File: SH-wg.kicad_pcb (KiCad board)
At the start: 4 copper layers, 54.6 x 99.2 mm, 83 parts, among them J101 Aux PCB Conn Male, J102 Aux PCB Conn Female, J201 Conn_01x05, J301 JTAG, J302 Digital IO, J303 Analog IO, J401 Power, J501 Conn_01x04, J701 Conn_02x03_Odd_Even, Q801 2N7002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

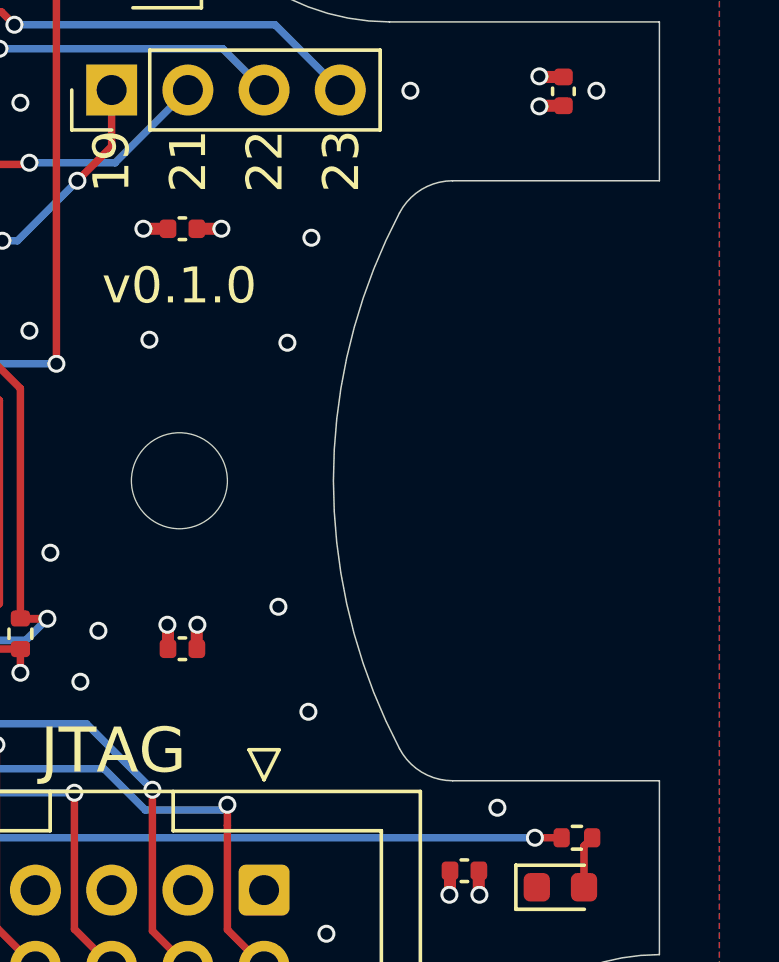
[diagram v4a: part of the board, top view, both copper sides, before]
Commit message: Add copper clearance around the mounting hole
Also make the M12 connector opening 1.5mm wider.
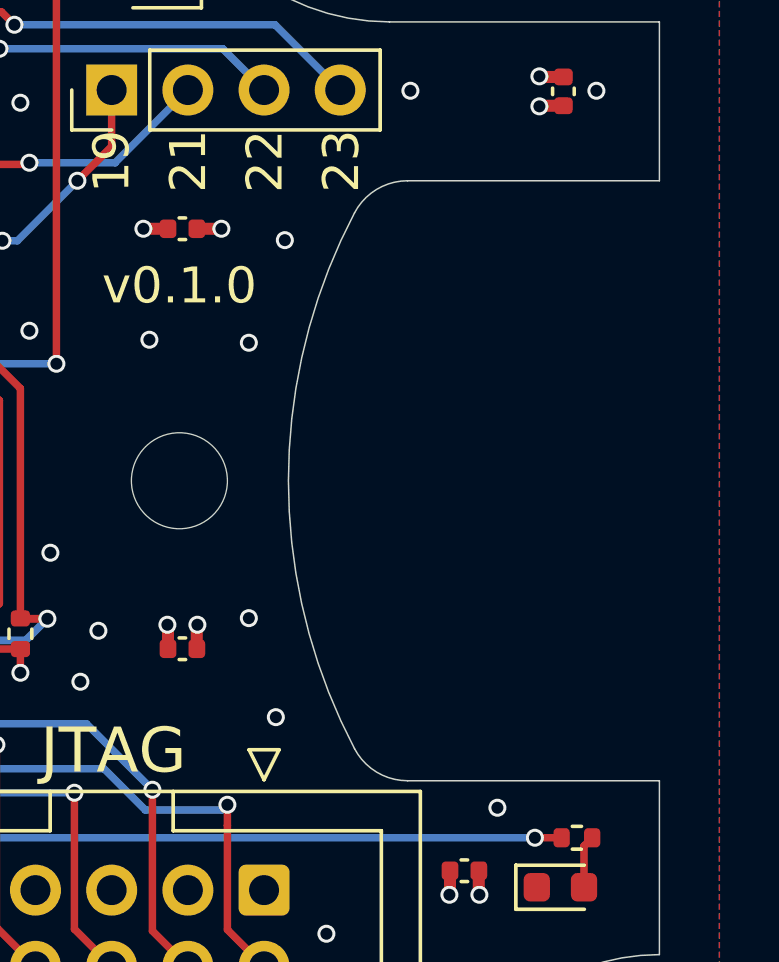
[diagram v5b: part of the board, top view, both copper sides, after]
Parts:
- H404: footprint MountingHole:MountingHole_3.2mm_M3 -> SH-wg:MountingHole_3.2mm_M3_no_copper
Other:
- outline, holes or cut-outs redrawn
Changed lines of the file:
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@@
     )
   )
-  (footprint "MountingHole:MountingHole_3.2mm_M3" (layer "F.Cu")
+  (footprint "SH-wg:MountingHole_3.2mm_M3_no_copper" (layer "F.Cu")
     (at 80.285 57.62)
     (descr "Mounting Hole 3.2mm, no annular, M3")
@@
     (fp_circle (center 0 0) (end 3.2 0) (layer "Cmts.User") (width 0.15) (fill none))
     (fp_circle (center 0 0) (end 3.45 0) (layer "F.CrtYd") (width 0.05) (fill none))
-    (pad "" np_thru_hole circle (at 0 0) (size 3.2 3.2) (drill 3.2) (layers *.Cu *.Mask))
+    (pad "" np_thru_hole circle (at 0 0) (size 3.2 3.2) (drill 3.2) (layers F&B.Cu *.Mask)
+      (solder_mask_margin 1.4) (clearance 1.6))
   )
   (footprint "Resistor_SMD:R_0402_1005Metric" (layer "F.Cu")
@@
   (gr_arc (start 96.285002 41.271847) (mid 98.29895 42.106052) (end 99.133155 44.12) (layer "Dwgs.User") (width 0.2))
   (gr_arc (start 87.285 41.271847) (mid 82.581434 39.323566) (end 80.633153 34.62) (layer "Dwgs.User") (width 0.2))
-  (gr_arc (start 87.622578 66.550309) (mid 85.419148 57.62) (end 87.622578 48.689691) (layer "Edge.Cuts") (width 0.05))
+  (gr_arc (start 86.122578 66.550309) (mid 83.919148 57.62) (end 86.122578 48.689691) (layer "Edge.Cuts") (width 0.05))
   (gr_line (start 43 116.62) (end 43 138.62) (layer "Edge.Cuts") (width 0.05))
   (gr_arc (start 44.285 72.914919) (mid 43.015801 72.389199) (end 42.490081 71.12) (layer "Edge.Cuts") (width 0.05))
@@
   (gr_arc (start 49.785 39.37) (mid 47.296537 41.183449) (end 44.285 41.825081) (layer "Edge.Cuts") (width 0.05))
   (gr_arc (start 89.079919 80.62) (mid 88.554199 81.889199) (end 87.285 82.414919) (layer "Edge.Cuts") (width 0.05))
-  (gr_arc (start 89.393037 67.62) (mid 88.358778 67.331814) (end 87.622578 66.550309) (layer "Edge.Cuts") (width 0.05))
+  (gr_arc (start 87.893037 67.62) (mid 86.858778 67.331814) (end 86.122578 66.550309) (layer "Edge.Cuts") (width 0.05))
   (gr_line (start 87.285 82.414919) (end 62.785 82.414919) (layer "Edge.Cuts") (width 0.05))
   (gr_arc (start 87.285 42.325081) (mid 83.940882 41.546238) (end 81.285 39.37) (layer "Edge.Cuts") (width 0.05))
   (gr_arc (start 53.285 72.914919) (mid 58.733315 75.171685) (end 60.990081 80.62) (layer "Edge.Cuts") (width 0.05))
   (gr_line (start 96.284999 67.62) (end 96.285 73.414919) (layer "Edge.Cuts") (width 0.05))
-  (gr_arc (start 87.622578 48.689691) (mid 88.358779 47.908186) (end 89.393037 47.62) (layer "Edge.Cuts") (width 0.05))
+  (gr_arc (start 86.122578 48.689691) (mid 86.858779 47.908186) (end 87.893037 47.62) (layer "Edge.Cuts") (width 0.05))
   (gr_arc (start 62.785 82.414919) (mid 61.515801 81.889199) (end 60.990081 80.62) (layer "Edge.Cuts") (width 0.05))
   (gr_line (start 97.08 116.62) (end 43 116.62) (layer "Edge.Cuts") (width 0.05))
@@
   (gr_line locked (start 49.785 39.37) (end 81.285 39.37) (layer "Edge.Cuts") (width 0.05))
   (gr_line (start 42.490081 71.12) (end 42.490081 43.62) (layer "Edge.Cuts") (width 0.05))
-  (gr_line (start 89.393037 67.62) (end 96.284999 67.62) (layer "Edge.Cuts") (width 0.05))
-  (gr_line (start 96.284999 47.62) (end 89.393037 47.62) (layer "Edge.Cuts") (width 0.05))
+  (gr_line (start 87.893037 67.62) (end 96.284999 67.62) (layer "Edge.Cuts") (width 0.05))
+  (gr_line (start 96.284999 47.62) (end 87.893037 47.62) (layer "Edge.Cuts") (width 0.05))
   (gr_text "SDA" (at 52.985 131.42 180) (layer "B.SilkS")
     (effects (font (size 0.8 0.8) (thickness 0.15)) (justify left mirror))
@@
   (via (at 60.485 75.22) (size 0.6) (drill 0.4) (layers "F.Cu" "B.Cu") (free) (net 1))
   (via (at 70.985 81.32) (size 0.6) (drill 0.4) (layers "F.Cu" "B.Cu") (free) (net 1))
-  (via (at 83.585 61.82) (size 0.6) (drill 0.4) (layers "F.Cu" "B.Cu") (free) (net 1))
+  (via (at 82.6 62.2) (size 0.6) (drill 0.4) (layers "F.Cu" "B.Cu") (free) (net 1))
   (via (at 58.085 60.82) (size 0.8) (drill 0.4) (layers "F.Cu" "B.Cu") (net 1))
   (via (at 68.585 49.92) (size 0.6) (drill 0.4) (layers "F.Cu" "B.Cu") (free) (net 1))
@@
   (via (at 92.285 45.14) (size 0.6) (drill 0.4) (layers "F.Cu" "B.Cu") (net 1))
   (via (at 50.485 50.62) (size 0.6) (drill 0.4) (layers "F.Cu" "B.Cu") (net 1))
-  (via (at 83.885 53.02) (size 0.6) (drill 0.4) (layers "F.Cu" "B.Cu") (free) (net 1))
+  (via (at 82.6 53.02) (size 0.6) (drill 0.4) (layers "F.Cu" "B.Cu") (free) (net 1))
   (via (at 80.285 79.62) (size 0.6) (drill 0.4) (layers "F.Cu" "B.Cu") (net 1))
   (via (at 62.285 51.72) (size 0.6) (drill 0.4) (layers "F.Cu" "B.Cu") (free) (net 1))
   (via (at 75.985 60.02) (size 0.6) (drill 0.4) (layers "F.Cu" "B.Cu") (free) (net 1))
   (via (at 89.285 71.42) (size 0.6) (drill 0.4) (layers "F.Cu" "B.Cu") (net 1))
-  (via (at 84.685 49.52) (size 0.6) (drill 0.4) (layers "F.Cu" "B.Cu") (free) (net 1))
+  (via (at 83.8 49.6) (size 0.6) (drill 0.4) (layers "F.Cu" "B.Cu") (free) (net 1))
   (via (at 70.585 63.82) (size 0.6) (drill 0.4) (layers "F.Cu" "B.Cu") (free) (net 1))
   (via (at 62.085 78.52) (size 0.6) (drill 0.4) (layers "F.Cu" "B.Cu") (free) (net 1))
@@
   (via (at 70.985 79.62) (size 0.6) (drill 0.4) (layers "F.Cu" "B.Cu") (net 1))
   (via (at 45.985 47.22) (size 0.6) (drill 0.4) (layers "F.Cu" "B.Cu") (net 1))
-  (via (at 84.585 65.32) (size 0.6) (drill 0.4) (layers "F.Cu" "B.Cu") (free) (net 1))
+  (via (at 83.5 65.5) (size 0.6) (drill 0.4) (layers "F.Cu" "B.Cu") (free) (net 1))
   (via (at 76.985 64.32) (size 0.6) (drill 0.4) (layers "F.Cu" "B.Cu") (free) (net 1))
   (via (at 79.085 49.22) (size 0.6) (drill 0.4) (layers "F.Cu" "B.Cu") (net 1))

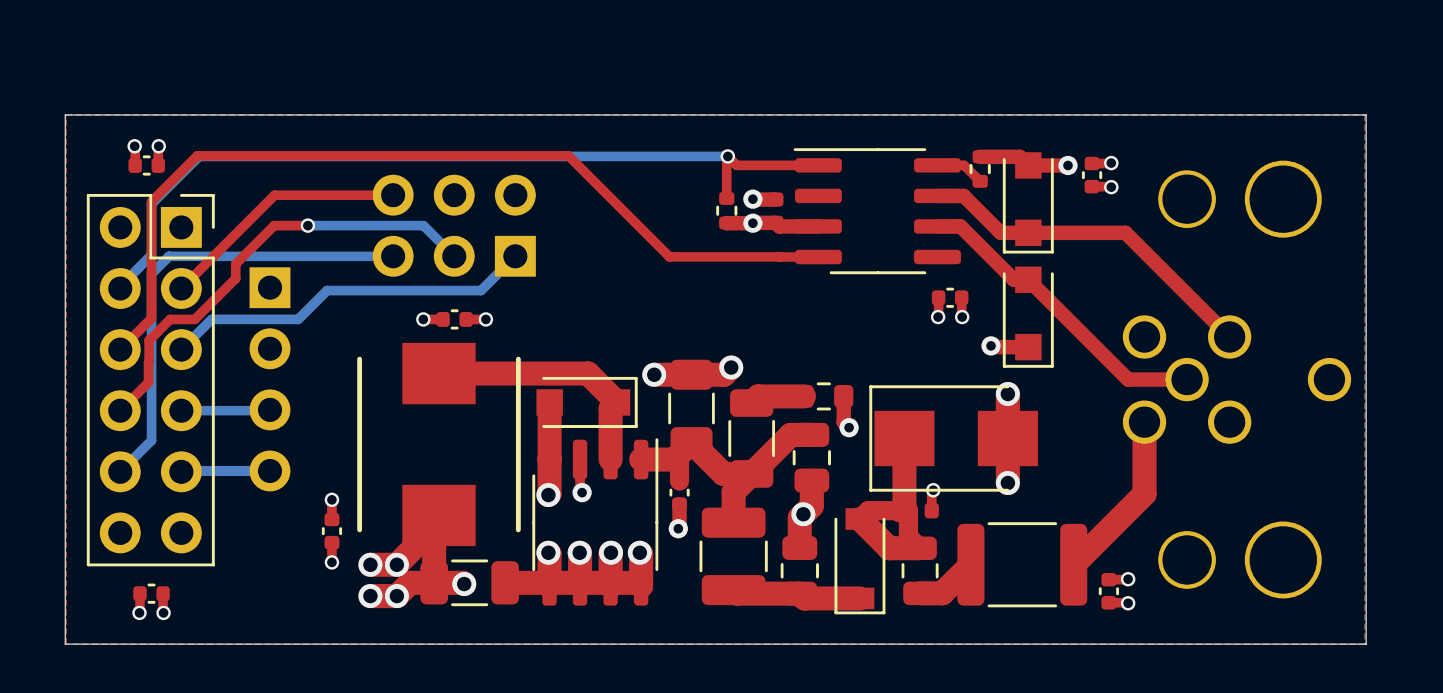
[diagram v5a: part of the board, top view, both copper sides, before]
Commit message: Update the design based on the test results
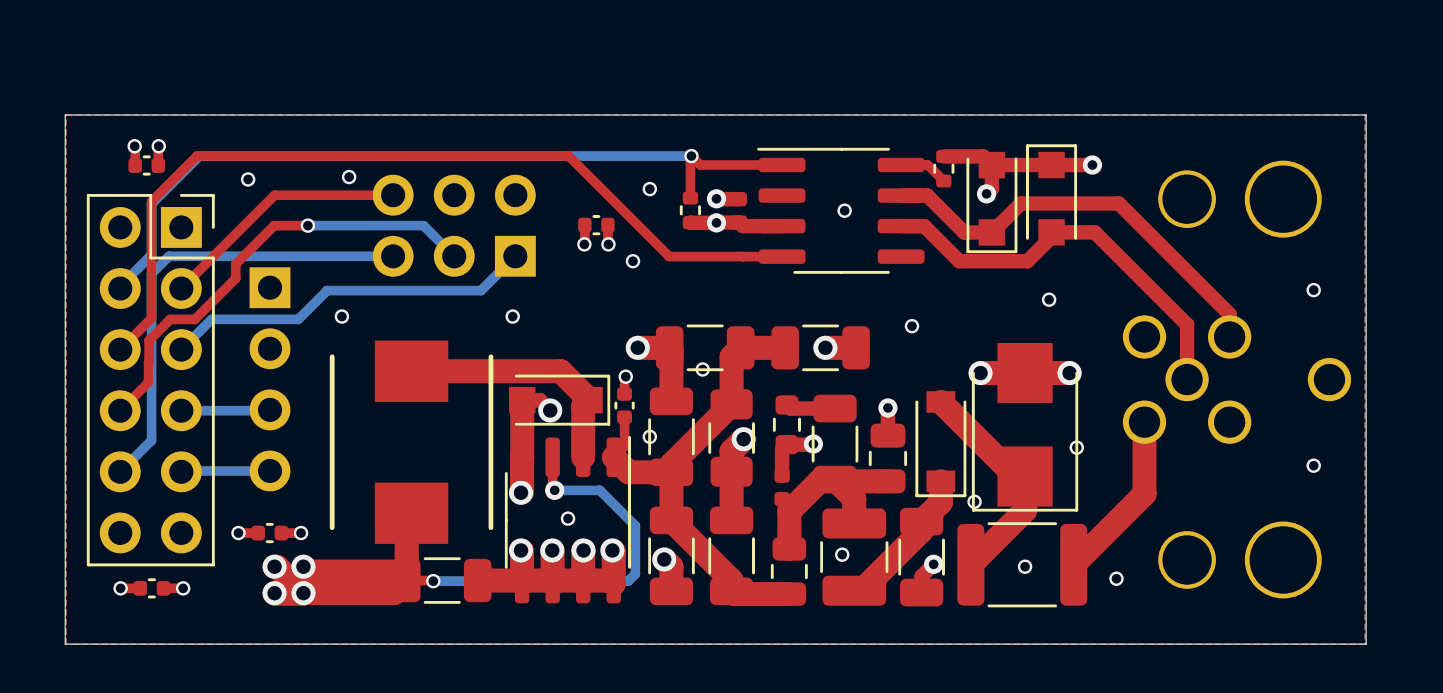
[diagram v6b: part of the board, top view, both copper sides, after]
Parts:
- removed C702, C703, C705: 100nF, Capacitor_SMD:C_0402_1005Metric
- added C608: 10uF/50V, Capacitor_SMD:C_1206_3216Metric, F.Cu at (69.6, 126.3)
- added C609: 10uF/50V, Capacitor_SMD:C_1206_3216Metric, F.Cu at (74.4, 126.3)
- added C610: 10uF/50V, Capacitor_SMD:C_1206_3216Metric, F.Cu at (70.7, 134.9)
- added C611: 10uF/50V, Capacitor_SMD:C_1206_3216Metric, F.Cu at (68.2, 130.0)
- added C612: 10uF/50V, Capacitor_SMD:C_1206_3216Metric, F.Cu at (68.2, 134.9)
- C601: value 470nF/50V -> 10uF/50V; footprint Capacitor_SMD:C_0805_2012Metric -> Capacitor_SMD:C_1206_3216Metric
- C602: value 10nF/50V -> 4.7nF/50V
- C605: value 22uF/35V -> 10uF/50V
- moved C704 15.0 mm to (65.1, 121.2)
- moved C707 11.7 mm to (51.5, 134.0)
- moved C701 7.85 mm to (46.6, 136.3), turned to 0 degrees
- moved D602 5.92 mm to (79.4, 130.2)
- moved C602 5.82 mm to (72.8, 132.1), turned to 90 degrees
- moved FB601 5.44 mm to (73.1, 135.6), turned to 90 degrees
- moved C601 5.10 mm to (78.6, 135.0), turned to 90 degrees
- moved L601 5.02 mm to (75.8, 135.0)
- moved D202 4.87 mm to (84.0, 120.1), turned to -90 degrees
- moved C606 4.28 mm to (66.2, 128.7), turned to 90 degrees
- moved C604 3.47 mm to (75.0, 130.3)
- moved C603 3.17 mm to (77.2, 130.9), turned to -90 degrees
- moved D601 2.92 mm to (82.9, 129.5), turned to 90 degrees
- moved C605 2.07 mm to (70.7, 130.1), turned to -90 degrees
- moved R601 1.94 mm to (73.0, 129.5), turned to 90 degrees
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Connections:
- C602 pad 1: /Power input/Vin_fused -> Net-(C602-Pad1)
- C603 pad 2: /Power input/IN -> Net-(C602-Pad1)
- C604 pad 1: /Power input/IN -> Net-(C602-Pad1)
- F601 pad 1: Net-(F601-Pad1) -> /Power input/Vin_fused
- FB601 pad 1: /Power input/Vin_fused -> /Power input/IN
- FB601 pad 2: Net-(F601-Pad1) -> Net-(C602-Pad1)
- L601 pad 2: /Power input/IN -> Net-(C602-Pad1)
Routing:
- net +3V3_1: track 21.9 -> 39.0 mm, vias 14 -> 11
- net Net-(C602-Pad1): track 0.00 -> 9.04 mm
- net /Power input/IN: track 12.8 -> 21.2 mm
- net GND1: track 40.5 -> 47.6 mm, vias 23 -> 42
- net /CAN bus/CAN_L: track 13.0 -> 17.0 mm
- net /CAN bus/CAN_H: track 14.6 -> 17.6 mm
- net Net-(F601-Pad1): track 2.60 -> 0.00 mm
- net /CAN_RX_1: track 36.9 -> 35.4 mm
- net /CAN_TX_1: track 34.5 -> 33.0 mm
- net /Power input/Vin_protected: track 5.39 -> 6.22 mm
- net /Power input/Vin_fused: track 9.99 -> 9.39 mm
